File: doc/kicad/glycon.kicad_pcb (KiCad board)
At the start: 2 copper layers, 96.5 x 73 mm, 21 parts, among them J1 2x20 Header, J2 USB_B, SW1 SW_Push, U0 Z80CPU, U1 628128_DIP32_SSOP32, U2 SST39SF010, U3 74HC32, U4 74HC86, X1 ACO-6.00MHz

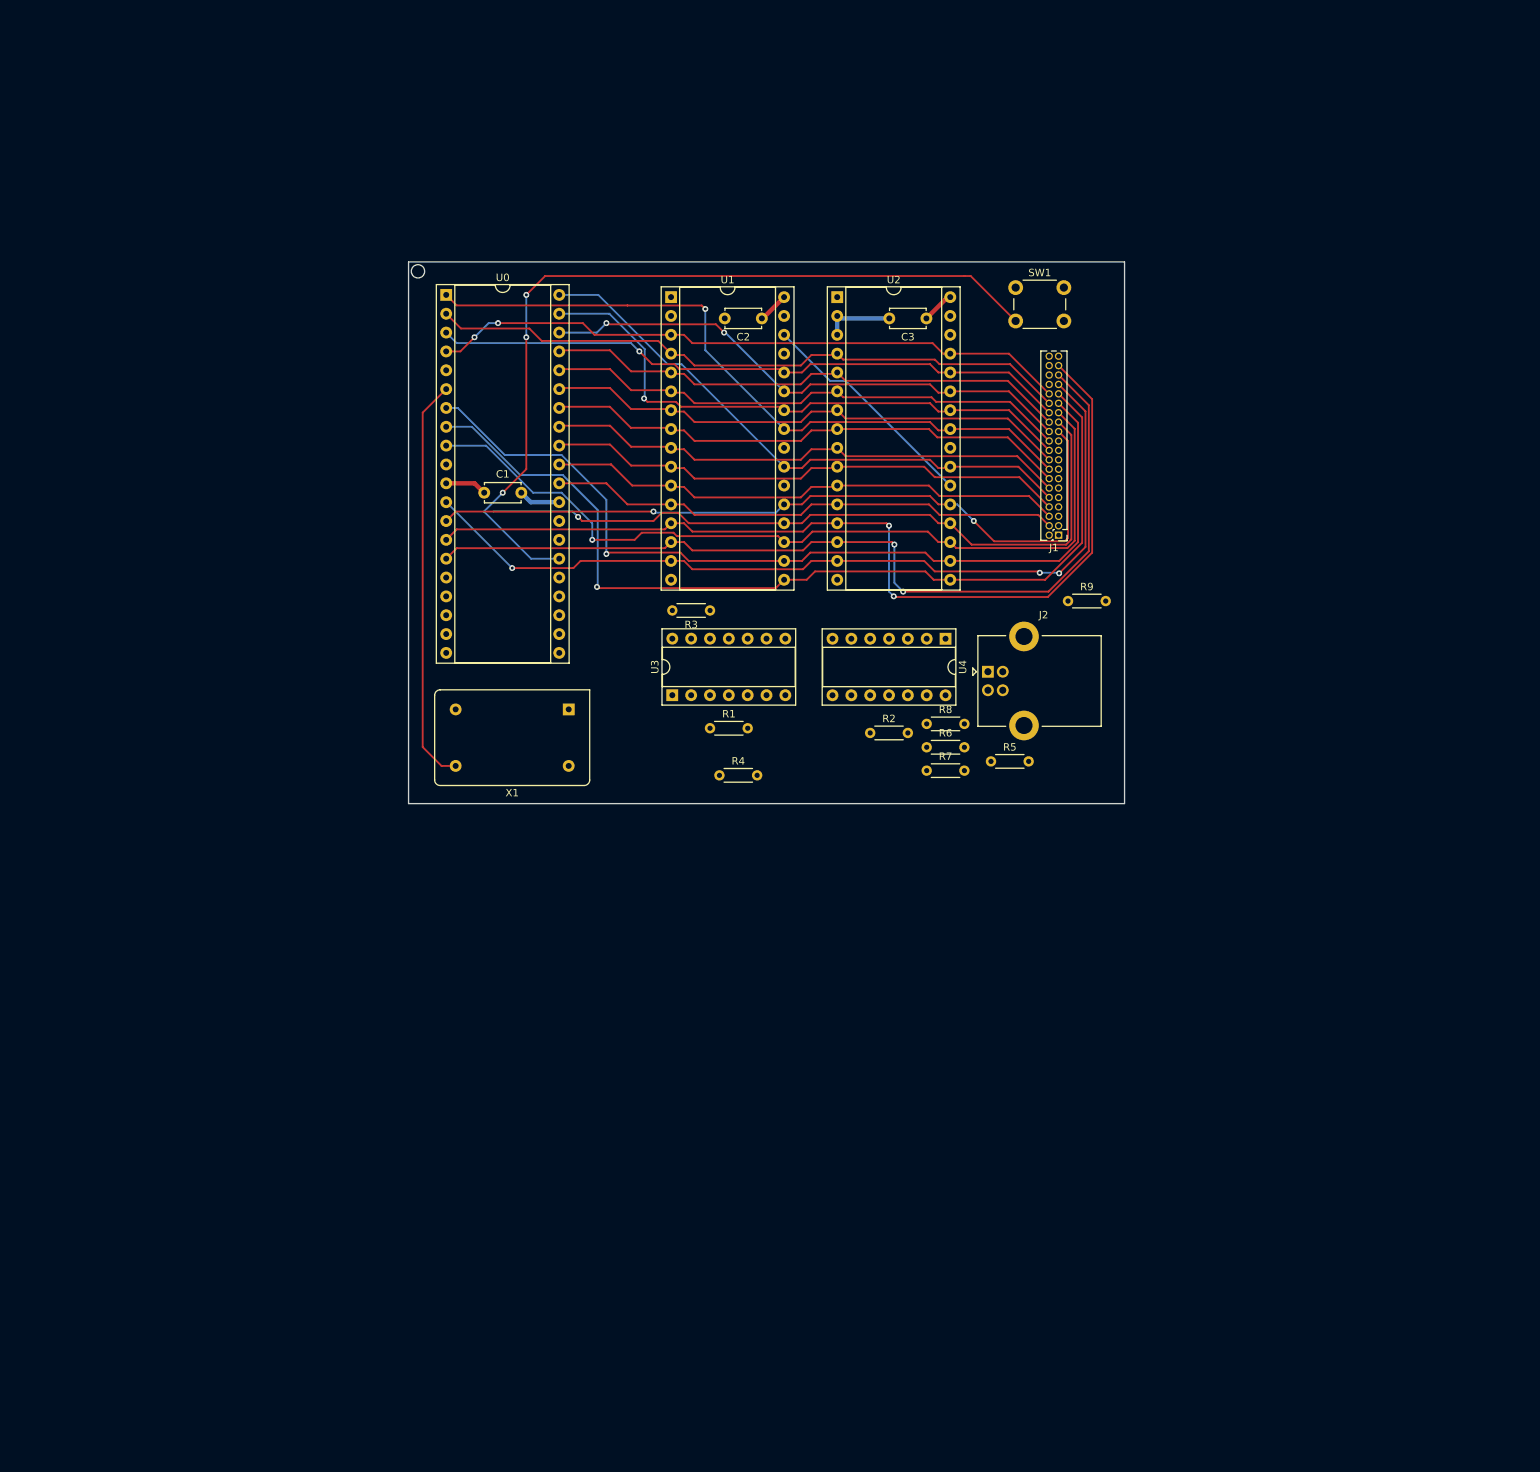
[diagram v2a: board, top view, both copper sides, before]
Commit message: expand schematic with IO devices/mainboard design
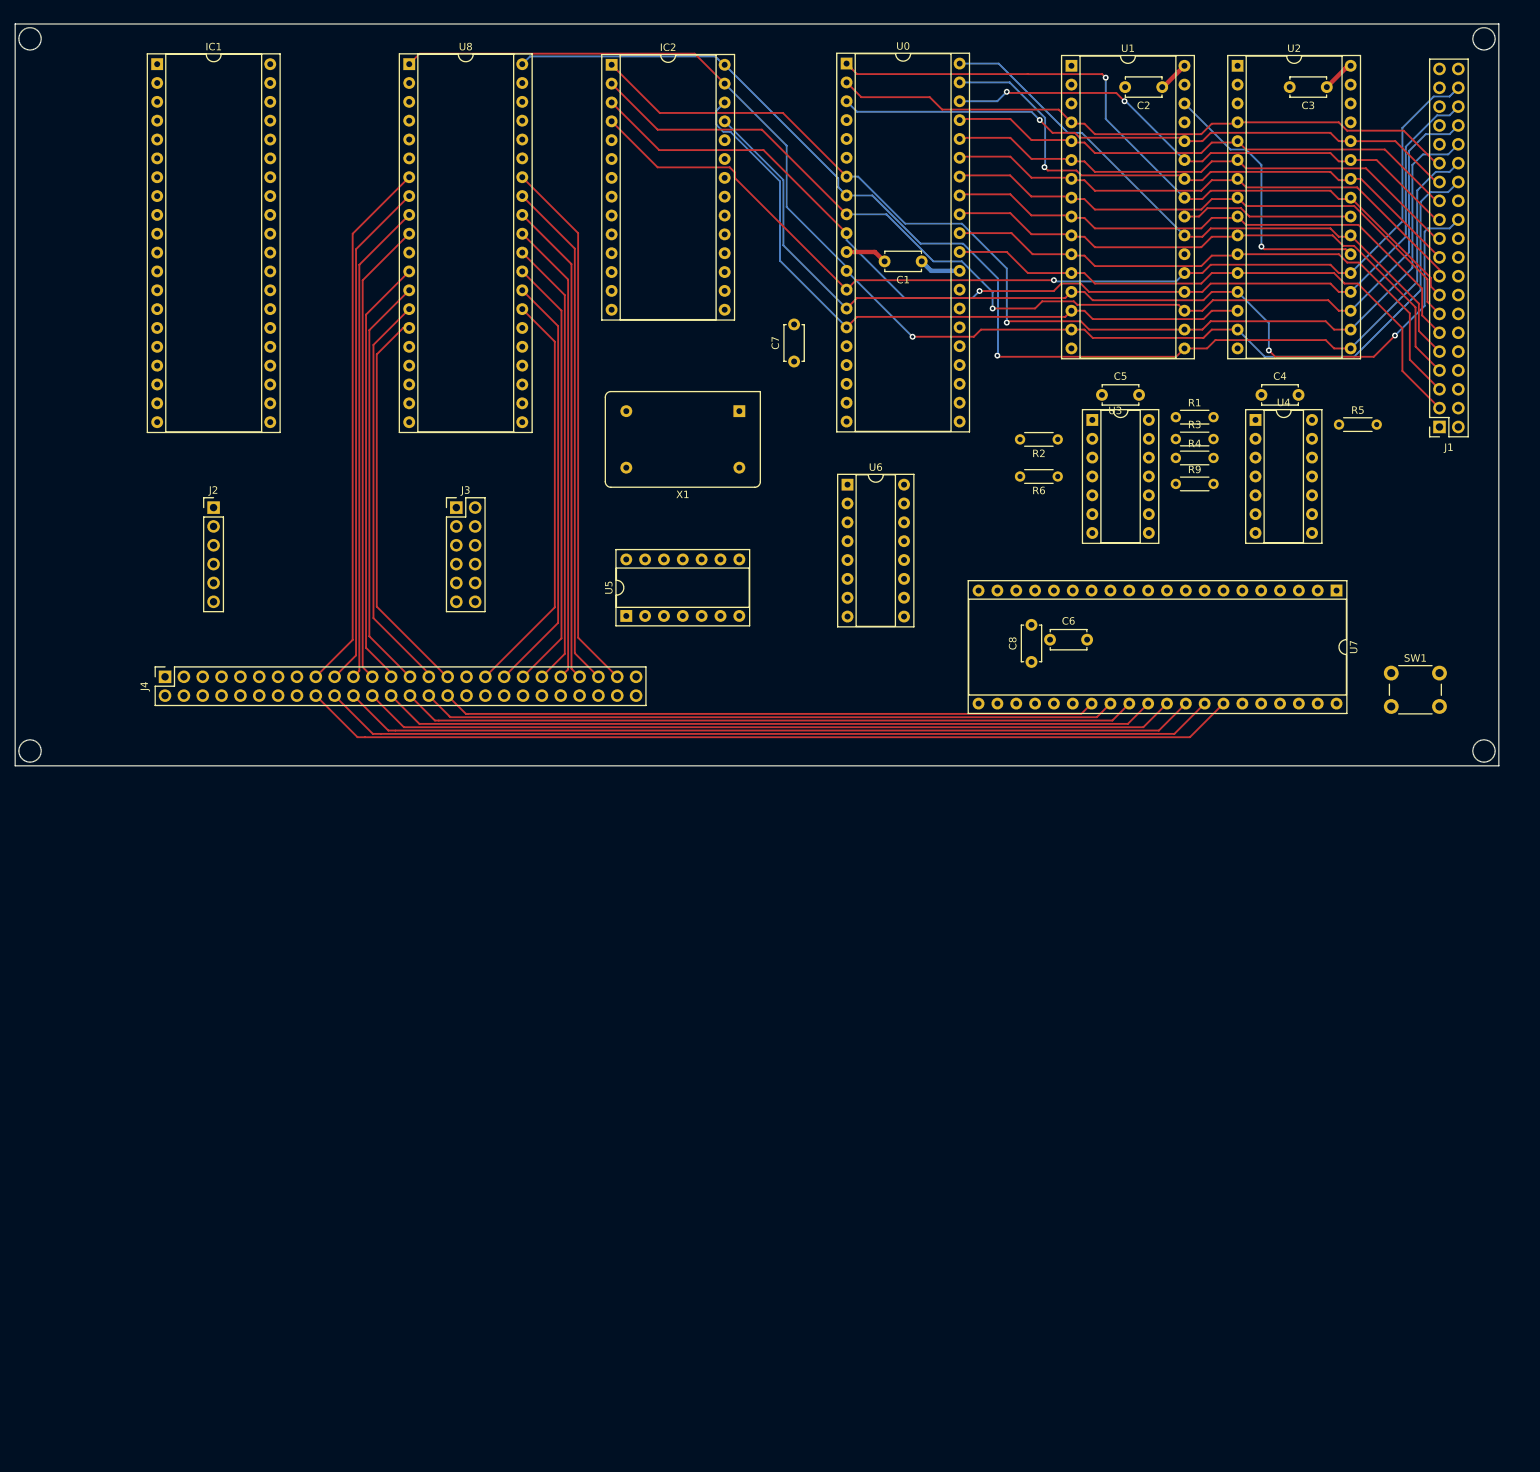
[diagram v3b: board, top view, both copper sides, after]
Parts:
- removed R7, R8: 10K, Resistor_THT:R_Axial_DIN0204_L3.6mm_D1.6mm_P5.08mm_Horizontal
- added C4: 100nF, Capacitor_THT:C_Disc_D4.7mm_W2.5mm_P5.00mm, F.Cu at (188.0, 70.0)
- added C5: 100nF, Capacitor_THT:C_Disc_D4.7mm_W2.5mm_P5.00mm, F.Cu at (166.5, 70.0)
- added C6: 100nF, Capacitor_THT:C_Disc_D4.7mm_W2.5mm_P5.00mm, F.Cu at (159.5, 103.0)
- added C7: 100nF, Capacitor_THT:C_Disc_D4.7mm_W2.5mm_P5.00mm, F.Cu at (125.0, 65.5)
- added C8: 100nF, Capacitor_THT:C_Disc_D4.7mm_W2.5mm_P5.00mm, F.Cu at (157.0, 106.0)
- added IC1: SIO0-DIP-40, Package_DIP:DIP-40_W15.24mm_Socket, F.Cu at (39.1, 25.4)
- added IC2: CTC-DIP-28, Package_DIP:DIP-28_W15.24mm_Socket, F.Cu at (100.4, 25.5)
- added J3: Int order hdr, Connector_PinHeader_2.54mm:PinHeader_2x06_P2.54mm_Vertical, F.Cu at (79.5, 85.2)
- added J4: Conn_02x26_Odd_Even, Connector_PinSocket_2.54mm:PinSocket_2x26_P2.54mm_Vertical, F.Cu at (40.2, 108.0)
- added U5: 74LS21, Package_DIP:DIP-14_W7.62mm_Socket, F.Cu at (102.4, 99.8)
- added U6: 74LS138, Package_DIP:DIP-16_W7.62mm_Socket, F.Cu at (132.2, 82.1)
- added U7: PIO-DIP-40, Package_DIP:DIP-40_W15.24mm_Socket, F.Cu at (198.1, 96.4)
- added U8: PIO-DIP-40, Package_DIP:DIP-40_W15.24mm_Socket, F.Cu at (73.1, 25.4)
- J1: value 2x20 Header -> Arduino/system bus header; footprint Connector_PinHeader_1.27mm:PinHeader_2x20_P1.27mm_Vertical -> Connector_PinSocket_2.54mm:PinSocket_2x20_P2.54mm_Vertical
- J2: value USB_B -> PMOD USBUART conn; footprint Connector_USB:USB_B_Lumberg_2411_02_Horizontal -> Connector_PinHeader_2.54mm:PinHeader_1x06_P2.54mm_Vertical
- U4: value 74HC86 -> 74HC04
- moved J2 106.7 mm to (46.7, 85.2)
- moved R1 75.5 mm to (176.5, 73.0)
- moved R4 74.9 mm to (176.5, 78.5)
- moved SW1 72.6 mm to (205.5, 107.5)
- moved U3 67.7 mm to (165.2, 73.4), turned to 0 degrees
- moved R3 66.9 mm to (176.5, 75.9), turned to 0 degrees
- moved C1 66.7 mm to (142.2, 52.0), turned to 180 degrees
- moved R5 65.3 mm to (198.5, 74.0)
- moved C2 62.3 mm to (174.6, 28.5)
- moved C3 62.3 mm to (196.8, 28.5)
- moved U0 62.3 mm to (132.1, 25.3)
- moved U1 62.3 mm to (162.4, 25.6)
- moved U2 62.3 mm to (184.8, 25.6)
- moved J1 53.4 mm to (212.0, 74.3)
- moved U4 51.1 mm to (187.2, 73.4), turned to 0 degrees
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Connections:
- J1 pad 1: /ROM WE -> VDD
- J1 pad 10: /A10 -> unconnected-(J1-Pin_10)
- J1 pad 11: unconnected-(J1-Pad11) -> A3
- J1 pad 12: /A3 -> unconnected-(J1-Pin_12)
- J1 pad 13: unconnected-(J1-Pad13) -> A4
- J1 pad 14: /A4 -> unconnected-(J1-Pin_14)
- J1 pad 15: unconnected-(J1-Pad15) -> A11
- J1 pad 16: /A11 -> unconnected-(J1-Pin_16)
- J1 pad 17: unconnected-(J1-Pad17) -> A5
- J1 pad 18: /A5 -> /~{IORQ}
- J1 pad 19: /RAM/ROM OE -> A9
- J1 pad 2: VDD -> /ROM WE
- J1 pad 20: /A9 -> /RAM/ROM OE
- J1 pad 21: /RAM WE -> A6
- J1 pad 22: /A6 -> /RAM WE
- J1 pad 23: /D7 -> A8
- J1 pad 24: /A8 -> /D0
- J1 pad 25: /D6 -> A7
- J1 pad 26: /A7 -> /D1
- J1 pad 27: /D5 -> A13
- J1 pad 28: /A13 -> /D2
- J1 pad 29: /D4 -> A12
- J1 pad 3: unconnected-(J1-Pad3) -> A0
- J1 pad 30: /A12 -> /D3
- J1 pad 31: /D3 -> A14
- J1 pad 32: /A14 -> /D4
- J1 pad 33: /D2 -> /A15
- J1 pad 34: /A15 -> /D5
- J1 pad 35: /D1 -> /BUSRQ
- J1 pad 36: Net-(J1-Pad36) -> /D6
- J1 pad 37: /D0 -> /BUSACK
- J1 pad 38: Net-(J1-Pad38) -> /D7
- J1 pad 39: Earth -> unconnected-(J1-Pin_39)
- J1 pad 4: /A0 -> unconnected-(J1-Pin_4)
- J1 pad 40: unconnected-(J1-Pad40) -> Earth
- J1 pad 5: unconnected-(J1-Pad5) -> A1
- J1 pad 6: /A1 -> unconnected-(J1-Pin_6)
- J1 pad 7: unconnected-(J1-Pad7) -> A2
- J1 pad 8: /A2 -> unconnected-(J1-Pin_8)
- J1 pad 9: unconnected-(J1-Pad9) -> A10
- J2 pad 1: VDD -> /RTSB
- J2 pad 2: unconnected-(J2-Pad2) -> /RxDB
- J2 pad 3: unconnected-(J2-Pad3) -> /TxDB
- J2 pad 4: Earth -> /CTSB
- R2 pad 1: Net-(R2-Pad1) -> /CLK
- R3 pad 1: Net-(R3-Pad1) -> Net-(U0-~{WR})
- R4 pad 1: Net-(R3-Pad1) -> Net-(U0-~{MREQ})
- R6 pad 1: Earth -> /RAM/ROM OE
- R6 pad 2: /A15 -> Earth
- R9 pad 2: Net-(J1-Pad38) -> /BUSRQ
- U0 pad 1: /A11 -> A11
- U0 pad 16: VDD -> /~{INT}
- U0 pad 19: Net-(R3-Pad1) -> Net-(U0-~{MREQ})
- U0 pad 2: /A12 -> A12
- U0 pad 20: unconnected-(U0-Pad20) -> /~{IORQ}
- U0 pad 21: Net-(R2-Pad1) -> /CLK
- U0 pad 22: Net-(R3-Pad1) -> Net-(U0-~{WR})
- U0 pad 23: Net-(U0-Pad23) -> /BUSACK
- U0 pad 24: VDD -> unconnected-(U0-~{WAIT})
- U0 pad 25: Net-(J1-Pad36) -> Net-(U0-~{BUSRQ})
- U0 pad 3: /A13 -> A13
- U0 pad 30: /A0 -> A0
- U0 pad 31: /A1 -> A1
- U0 pad 32: /A2 -> A2
- U0 pad 33: /A3 -> A3
- U0 pad 34: /A4 -> A4
- U0 pad 35: /A5 -> A5
- U0 pad 36: /A6 -> A6
- U0 pad 37: /A7 -> A7
- U0 pad 38: /A8 -> A8
- U0 pad 39: /A9 -> A9
- U0 pad 4: /A14 -> unconnected-(U0-A14)
- U0 pad 40: /A10 -> A10
- U0 pad 5: Net-(R7-Pad2) -> /A15
- U0 pad 6: Net-(U0-Pad6) -> /CLK
- U1 pad 10: /A2 -> A2
- U1 pad 11: /A1 -> A1
- U1 pad 12: /A0 -> A0
- U1 pad 2: VDD -> /RAM_PGA2
- U1 pad 23: /A10 -> A10
- U1 pad 24: Net-(U1-Pad24) -> /~{MEMRD}
- U1 pad 25: /A11 -> A11
- U1 pad 26: /A9 -> A9
- U1 pad 27: /A8 -> A8
- U1 pad 28: /A13 -> A13
- U1 pad 3: /A14 -> /RAM_PGA0
- U1 pad 30: Net-(U1-Pad30) -> /A15
- U1 pad 31: VDD -> /RAM_PGA1
- U1 pad 4: /A12 -> A12
- U1 pad 5: /A7 -> A7
- U1 pad 6: /A6 -> A6
- U1 pad 7: /A5 -> A5
- U1 pad 8: /A4 -> A4
- U1 pad 9: /A3 -> A3
- U2 pad 10: /A2 -> A2
- U2 pad 11: /A1 -> A1
- U2 pad 12: /A0 -> A0
- U2 pad 2: Earth -> /ROM_PGA2
- U2 pad 22: Net-(U1-Pad30) -> /A15
- U2 pad 23: /A10 -> A10
- U2 pad 24: Net-(U1-Pad24) -> /~{MEMRD}
- U2 pad 25: /A11 -> A11
- U2 pad 26: /A9 -> A9
- U2 pad 27: /A8 -> A8
- U2 pad 28: /A13 -> A13
- U2 pad 29: /A14 -> /ROM_PGA0
- U2 pad 3: Earth -> /ROM_PGA1
- U2 pad 31: Net-(U2-Pad31) -> Net-(U2-~{WE})
- U2 pad 4: /A12 -> A12
- U2 pad 5: /A7 -> A7
- U2 pad 6: /A6 -> A6
- U2 pad 7: /A5 -> A5
- U2 pad 8: /A4 -> A4
- U2 pad 9: /A3 -> A3
- U3 pad 1: Net-(R3-Pad1) -> Net-(U0-~{MREQ})
- U3 pad 12: Net-(R3-Pad1) -> Net-(U0-~{MREQ})
- U3 pad 13: Net-(R3-Pad1) -> Net-(U0-~{WR})
- U3 pad 2: Net-(R2-Pad1) -> /CLK
- U3 pad 4: Net-(R7-Pad2) -> /RAM/ROM OE
- U3 pad 5: /A15 -> Net-(U3-Pad3)
- U3 pad 6: Net-(U1-Pad30) -> /~{MEMRD}
- U4 pad 1: /RAM/ROM OE -> /ROM WE
- U4 pad 10: Net-(J1-Pad38) -> (no net)
- U4 pad 2: Net-(U3-Pad3) -> Net-(U2-~{WE})
- U4 pad 3: Net-(U1-Pad24) -> /BUSRQ
- U4 pad 4: VDD -> Net-(U0-~{BUSRQ})
- U4 pad 5: /ROM WE -> (no net)
- U4 pad 6: Net-(U2-Pad31) -> (no net)
- U4 pad 8: Net-(U0-Pad23) -> (no net)
- U4 pad 9: VDD -> (no net)
- X1 pad 8: Net-(U0-Pad6) -> /CLK
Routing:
- net /PC7: track 0.00 -> 126.6 mm
- net /PC6: track 0.00 -> 121.1 mm
- net /PC5: track 0.00 -> 115.7 mm
- net Net-(U0-~{RESET}): track 113.9 -> 0.00 mm, vias 3 -> 0
- net /PC4: track 0.00 -> 110.2 mm
- net /PC3: track 0.00 -> 104.8 mm
- net /PC2: track 0.00 -> 99.3 mm
- net A11: track 0.00 -> 97.7 mm, vias 0 -> 1
- net /A11: track 95.2 -> 0.00 mm, vias 1 -> 0
- net /PC1: track 0.00 -> 93.9 mm
- net /PC0: track 0.00 -> 88.4 mm
- net /A12: track 87.5 -> 0.00 mm
- net /A14: track 86.8 -> 0.00 mm, vias 2 -> 0
- net /A13: track 86.7 -> 0.00 mm, vias 1 -> 0
- net A12: track 0.00 -> 85.0 mm
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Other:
- board size 96.5 x 73 mm -> 200 x 100 mm

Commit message: more schematic work
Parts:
- removed U5: 74LS21, Package_DIP:DIP-14_W7.62mm_Socket
- removed U8: PIO-DIP-40, Package_DIP:DIP-40_W15.24mm_Socket
- added C10: 100nF, Capacitor_THT:C_Disc_D4.7mm_W2.5mm_P5.00mm, F.Cu at (91.3, 207.7)
- added C11: 100nF, Capacitor_THT:C_Disc_D4.7mm_W2.5mm_P5.00mm, F.Cu at (91.3, 211.8)
- added C7: 100nF, Capacitor_THT:C_Disc_D4.7mm_W2.5mm_P5.00mm, F.Cu at (149.1, 152.3)
- added C9: 100nF, Capacitor_THT:C_Disc_D4.7mm_W2.5mm_P5.00mm, F.Cu at (99.5, 204.8)
- added R7: 10K, Resistor_THT:R_Axial_DIN0204_L3.6mm_D1.6mm_P5.08mm_Horizontal, F.Cu at (157.1, 151.8)
- added U10: 74HC244, Package_DIP:DIP-20_W7.62mm_Socket, F.Cu at (135.1, 151.0)
- added U11: PIO-DIP-40, Package_DIP:DIP-40_W15.24mm_Socket, F.Cu at (198.0, 95.8)
- added U12: 74LS21, Package_DIP:DIP-14_W7.62mm_Socket, F.Cu at (101.5, 97.0)
- added U9: 74HC244, Package_DIP:DIP-20_W7.62mm_Socket, F.Cu at (119.2, 151.0)
- J4: value Conn_02x26_Odd_Even -> Conn_02x21_Odd_Even; footprint Connector_PinSocket_2.54mm:PinSocket_2x26_P2.54mm_Vertical -> Connector_PinHeader_2.54mm:PinHeader_2x21_P2.54mm_Vertical
- SW1: value SW_Push -> SW_Push_Open
- U6: value 74LS138 -> 74LS139
- U7: value PIO-DIP-40 -> SIO0-DIP-40
- moved U7 143.7 mm to (72.9, 25.9), turned to 0 degrees
- moved U6 87.1 mm to (152.3, 166.9)
- moved J4 13.8 mm to (53.8, 109.7)
- moved SW1 2.02 mm to (206.2, 105.6)
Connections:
- net A10 renamed /A10
- net A11 renamed /A11
- net A12 renamed /A12
- net A13 renamed /A13
- net A5 renamed /A5
- net A6 renamed /A6
- net A7 renamed /A7
- net A8 renamed /A8
- net A9 renamed /A9
- C3 pad 1: VDD -> Earth
- C3 pad 2: Earth -> VDD
- C8 pad 1: VCC -> VDD
- IC2 pad 14: unconnected-(IC2-~{M1}) -> /~{M1}
- IC2 pad 17: unconnected-(IC2-~{RESET}) -> /~{RESET}
- IC2 pad 18: A0 -> /A0
- IC2 pad 19: A1 -> /A1
- IC2 pad 24: VCC -> VDD
- J1 pad 11: A3 -> /A3
- J1 pad 13: A4 -> /A4
- J1 pad 16: unconnected-(J1-Pin_16) -> /~{M1}
- J1 pad 3: A0 -> /A0
- J1 pad 31: A14 -> /PGA0
- J1 pad 33: /A15 -> /PGA1
- J1 pad 39: unconnected-(J1-Pin_39) -> /~{INTIN}
- J1 pad 4: unconnected-(J1-Pin_4) -> /RESET
- J1 pad 5: A1 -> /A1
- J1 pad 7: A2 -> /A2
- J3 pad 1: VCC -> VDD
- J3 pad 11: VCC -> VDD
- J3 pad 12: VCC -> VDD
- J3 pad 2: VCC -> VDD
- J4 pad 1: VCC -> VDD
- J4 pad 10: unconnected-(J4-Pin_10) -> /PC2
- J4 pad 12: unconnected-(J4-Pin_12) -> /PC1
- J4 pad 13: unconnected-(J4-Pin_13) -> /CLK
- J4 pad 14: unconnected-(J4-Pin_14) -> /PC0
- J4 pad 15: VCC -> VDD
- J4 pad 18: /PC7 -> /PB0
- J4 pad 20: /PC6 -> /PB1
- J4 pad 22: /PC5 -> /PB2
- J4 pad 24: /PC4 -> /PB3
- J4 pad 26: /PC3 -> /PB4
- J4 pad 28: /PC2 -> /PB5
- J4 pad 30: /PC1 -> /PB6
- J4 pad 32: /PC0 -> /PB7
- J4 pad 33: VCC -> /~{RTSA}
- J4 pad 34: Earth -> /TXDA
- J4 pad 35: /PB0 -> /~{CTSA}
- J4 pad 36: unconnected-(J4-Pin_36) -> /SERCLK
- J4 pad 37: /PB1 -> /~{DTRA}
- J4 pad 38: unconnected-(J4-Pin_38) -> /SYNCA
- J4 pad 39: /PB2 -> /~{DCDA}
- J4 pad 4: unconnected-(J4-Pin_4) -> /RESET
- J4 pad 40: unconnected-(J4-Pin_40) -> /~{W}/~{RDYA}
- J4 pad 41: /PB3 -> VDD
- J4 pad 42: unconnected-(J4-Pin_42) -> Earth
- J4 pad 8: unconnected-(J4-Pin_8) -> /PC3
- R1 pad 1: VDD -> /~{RESET}
- R1 pad 2: Net-(U0-~{RESET}) -> Earth
- SW1 pad 1: Earth -> Net-(SW1-A)
- SW1 pad 2: Net-(U0-~{RESET}) -> /~{RESET}
- U0 pad 26: Net-(U0-~{RESET}) -> /~{RESET}
- U0 pad 27: unconnected-(U0-~{M1}) -> /~{M1}
- U0 pad 30: A0 -> /A0
- U0 pad 31: A1 -> /A1
- U0 pad 32: A2 -> /A2
- U0 pad 33: A3 -> /A3
- U0 pad 34: A4 -> /A4
- U0 pad 4: unconnected-(U0-A14) -> /PGA0
- U0 pad 5: /A15 -> /PGA1
- U1 pad 10: A2 -> /A2
- U1 pad 11: A1 -> /A1
- U1 pad 12: A0 -> /A0
- U1 pad 2: /RAM_PGA2 -> /A16
- U1 pad 22: Earth -> VDD
- U1 pad 3: /RAM_PGA0 -> /A14
- U1 pad 30: /A15 -> /A18
- U1 pad 31: /RAM_PGA1 -> /A15
- U1 pad 8: A4 -> /A4
- U1 pad 9: A3 -> /A3
- U2 pad 10: A2 -> /A2
- U2 pad 11: A1 -> /A1
- U2 pad 12: A0 -> /A0
- U2 pad 2: /ROM_PGA2 -> /A16
- U2 pad 22: /A15 -> unconnected-(U2-~{CE})
- U2 pad 29: /ROM_PGA0 -> /A14
- U2 pad 3: /ROM_PGA1 -> /A15
- U2 pad 8: A4 -> /A4
- U2 pad 9: A3 -> /A3
- U4 pad 5: (no net) -> /RESET
- U4 pad 6: (no net) -> Net-(SW1-A)
- U6 pad 1: A2 -> VDD
- U6 pad 10: unconnected-(U6-O5) -> Net-(U6B-O2)
- U6 pad 11: unconnected-(U6-O4) -> Net-(IC2-~{CE})
- U6 pad 12: /CLK -> Net-(U11-~{CE})
- U6 pad 13: Net-(IC2-~{CE}) -> /A3
- U6 pad 14: Net-(U6-O1) -> /A2
- U6 pad 15: Net-(U6-O0) -> VDD
- U6 pad 16: Earth -> VDD
- U6 pad 2: A3 -> /PGA1
- U6 pad 3: A4 -> /PGA0
- U6 pad 4: Earth -> Net-(U10-2OE)
- U6 pad 5: Earth -> Net-(U10-1OE)
- U6 pad 6: VCC -> Net-(U6A-O2)
- U6 pad 7: unconnected-(U6-O7) -> Net-(U6A-O3)
- U6 pad 8: VCC -> Earth
- U6 pad 9: unconnected-(U6-O6) -> Net-(U6B-O3)
- U7 pad 1: /D2 -> /D1
- U7 pad 10: /ROM_PGA1 -> /~{W}/~{RDYA}
- U7 pad 11: Earth -> /SYNCA
- U7 pad 12: /ROM_PGA0 -> unconnected-(U7-RXDA)
- U7 pad 13: /RAM_PGA2 -> /SERCLK
- U7 pad 14: /RAM_PGA1 -> /SERCLK
- U7 pad 15: /RAM_PGA0 -> /TXDA
- U7 pad 16: unconnected-(U7-~{ASTB}) -> /~{DTRA}
- U7 pad 17: unconnected-(U7-~{BSTB}) -> /~{RTSA}
- U7 pad 18: unconnected-(U7-ARDY) -> /~{CTSA}
- U7 pad 19: /D0 -> /~{DCDA}
- U7 pad 2: /D7 -> /D3
- U7 pad 20: /D1 -> /CLK
- U7 pad 21: unconnected-(U7-BRDY) -> /~{RESET}
- U7 pad 22: /IEO1 -> unconnected-(U7-~{DCDB})
- U7 pad 23: Net-(U7-~{INT}) -> /CTSB
- U7 pad 24: /IEI1 -> /RTSB
- U7 pad 25: /CLK -> unconnected-(U7-~{DTRB})
- U7 pad 26: VCC -> /TxDB
- U7 pad 27: /PC0 -> /SERCLK
- U7 pad 28: /PC1 -> /RxDB
- U7 pad 29: /PC2 -> unconnected-(U7-~{SYNCB})
- U7 pad 3: /D6 -> /D5
- U7 pad 30: /PC3 -> unconnected-(U7-~{W}/~{RDYB})
- U7 pad 31: /PC4 -> Earth
- U7 pad 32: /PC5 -> /CLK
- U7 pad 33: /PC6 -> /A1
- U7 pad 34: /PC7 -> /A0
- U7 pad 35: /CLK -> Net-(U6B-O3)
- U7 pad 37: /~{M1} -> /D6
- U7 pad 38: /D5 -> /D4
- U7 pad 39: /D4 -> /D2
- U7 pad 4: Net-(U6-O0) -> /D7
- U7 pad 40: /D3 -> /D0
- U7 pad 5: A1 -> Net-(U7-~{INT})
- U7 pad 6: A0 -> /IEI2
- U7 pad 7: unconnected-(U7-PA7) -> /IEO2
- U7 pad 8: unconnected-(U7-PA6) -> /~{M1}
- U7 pad 9: /ROM_PGA2 -> VDD
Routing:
- net /SERCLK: track 0.00 -> 166.5 mm
- net /A0: track 0.00 -> 150.6 mm
- net /A1: track 0.00 -> 147.3 mm
- net /PC7: track 126.6 -> 0.00 mm
- net /PC6: track 121.1 -> 0.00 mm
- net /PC5: track 115.7 -> 0.00 mm
- net /PC4: track 110.2 -> 0.00 mm
- net Net-(U10-1A3): track 0.00 -> 104.8 mm
- net Net-(U10-1A2): track 0.00 -> 99.3 mm
- net Net-(U10-1A1): track 0.00 -> 93.9 mm
- net Net-(U10-1A0): track 0.00 -> 88.4 mm
- net A1: track 78.2 -> 0.00 mm
- net A0: track 78.0 -> 0.00 mm
- net A2: track 77.7 -> 0.00 mm
- net /A2: track 0.00 -> 77.7 mm
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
